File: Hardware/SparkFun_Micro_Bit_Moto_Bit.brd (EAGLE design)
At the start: 58.4 x 76.2 mm, 104 parts, among them J1 POWER_JACKPTH_LOCK, J2 CORTEX_DEBUGPTH, U1 CY8C4245LQI-483, U2 TPS62172, U3 micro:bit, U4 DRV8835

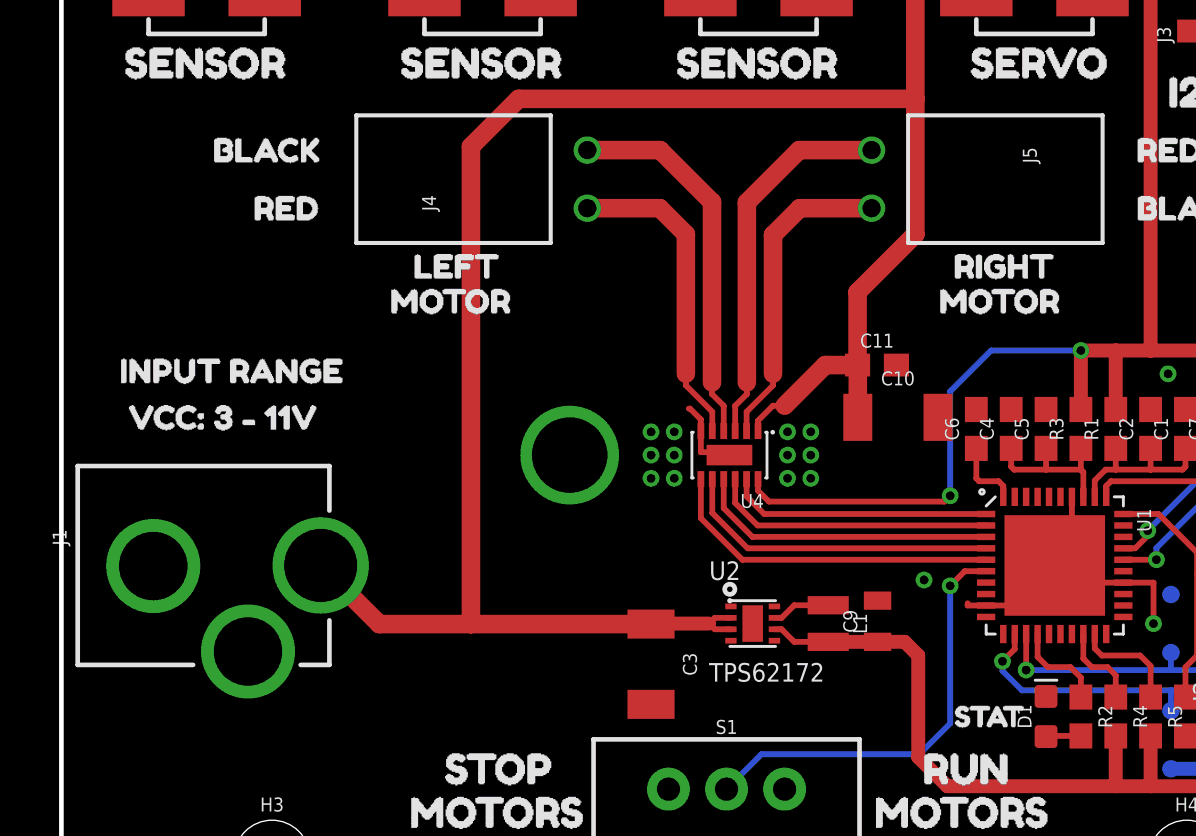
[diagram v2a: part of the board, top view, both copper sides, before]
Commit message: v20 update
Updated LED to current footprint and moved barrel connector in to reduce overhanging parts
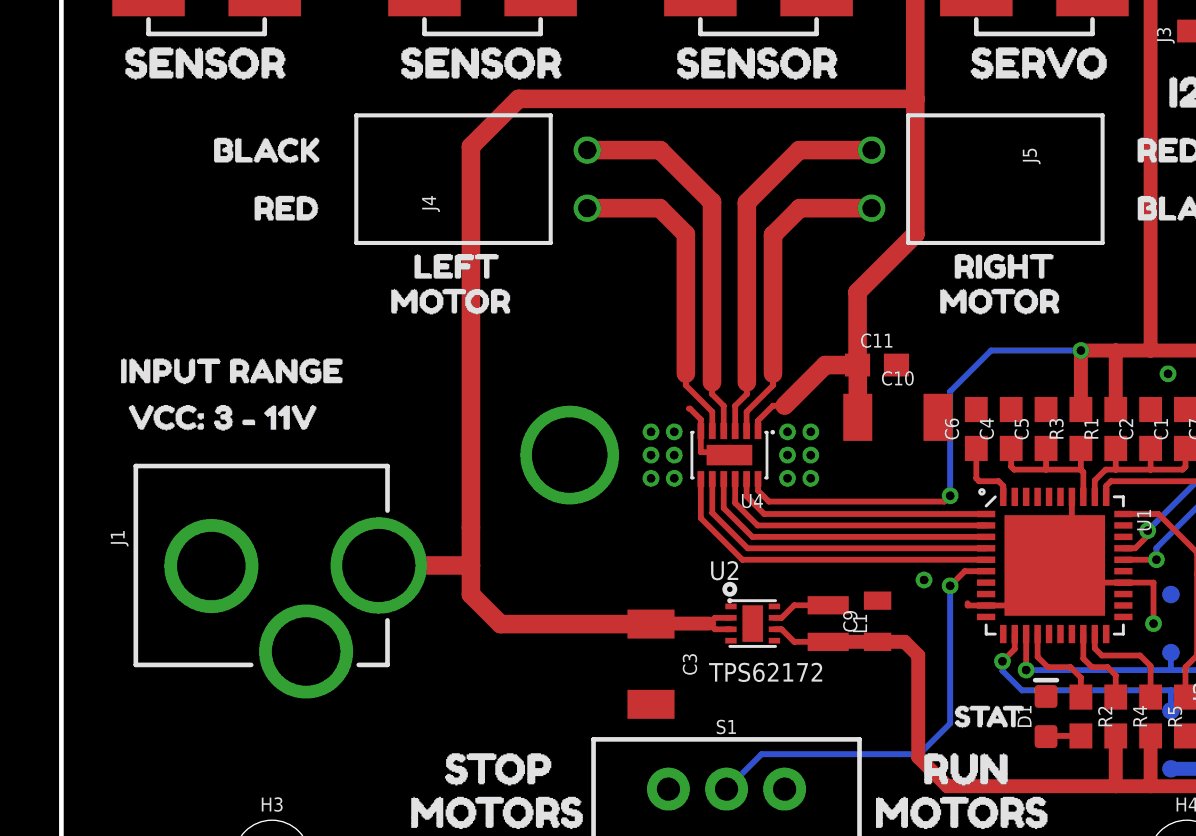
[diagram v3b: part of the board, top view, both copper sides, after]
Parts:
- moved J1 2.54 mm to (0.00, 18.7)
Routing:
- net VCC: track 95.9 -> 91.6 mm
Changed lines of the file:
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@@
 <layer number="38" name="bTest" color="7" fill="1" visible="no" active="yes"/>
 <layer number="39" name="tKeepout" color="4" fill="11" visible="yes" active="yes"/>
-<layer number="40" name="bKeepout" color="1" fill="11" visible="no" active="yes"/>
+<layer number="40" name="bKeepout" color="1" fill="11" visible="yes" active="yes"/>
 <layer number="41" name="tRestrict" color="4" fill="10" visible="no" active="yes"/>
 <layer number="42" name="bRestrict" color="1" fill="10" visible="no" active="yes"/>
@@
 <attribute name="VALUE" x="30.72" y="25.273" size="0.6096" layer="27" font="vector" ratio="20" rot="R180" align="top-left"/>
 </element>
-<element name="J1" library="SparkFun-Connectors" package="POWER_JACK_PTH_LOCK" value="POWER_JACKPTH_LOCK" x="-2.54" y="18.669" smashed="yes" rot="R270">
-<attribute name="NAME" x="-0.381" y="20.2438" size="0.6096" layer="25" font="vector" ratio="20" rot="R270"/>
-<attribute name="PROD_ID" value="CONN-08197" x="-27.94" y="56.769" size="1.778" layer="27" font="vector" ratio="15" rot="R270" display="off"/>
-<attribute name="SF_ID" value="PRT-00119" x="-27.94" y="56.769" size="1.778" layer="27" font="vector" ratio="15" rot="R270" display="off"/>
-<attribute name="VALUE" x="-1.397" y="20.574" size="0.6096" layer="27" font="vector" ratio="20" rot="R270"/>
+<element name="J1" library="SparkFun-Connectors" package="POWER_JACK_PTH_LOCK" value="POWER_JACKPTH_LOCK" x="0" y="18.669" smashed="yes" rot="R270">
+<attribute name="NAME" x="2.159" y="20.2438" size="0.6096" layer="25" font="vector" ratio="20" rot="R270"/>
+<attribute name="PROD_ID" value="CONN-08197" x="-25.4" y="56.769" size="1.778" layer="27" font="vector" ratio="15" rot="R270" display="off"/>
+<attribute name="SF_ID" value="PRT-00119" x="-25.4" y="56.769" size="1.778" layer="27" font="vector" ratio="15" rot="R270" display="off"/>
+<attribute name="VALUE" x="1.143" y="20.574" size="0.6096" layer="27" font="vector" ratio="20" rot="R270"/>
 </element>
 <element name="U2" library="SparkFun-IC-Power" package="WSON-8-PAD" value="TPS62172" x="30.226" y="16.129" smashed="yes" rot="R270">
@@
 <wire x1="37.338" y1="39.070753125" x2="19.990490625" y2="39.070753125" width="0.8128" layer="1"/>
 <wire x1="19.990490625" y1="39.070753125" x2="17.907" y2="36.9872625" width="0.8128" layer="1"/>
-<wire x1="17.907" y1="36.9872625" x2="17.907" y2="16.106" width="0.8128" layer="1"/>
+<wire x1="17.907" y1="36.9872625" x2="17.907" y2="20.32" width="0.8128" layer="1"/>
 <contactref element="J9" pad="4"/>
 <contactref element="C11" pad="1"/>
 <contactref element="U4" pad="1"/>
 <contactref element="C10" pad="1"/>
+<wire x1="25.781" y1="16.106" x2="19.2" y2="16.106" width="0.8128" layer="1"/>
+<wire x1="19.2" y1="16.106" x2="17.907" y2="17.399" width="0.8128" layer="1"/>
+<wire x1="17.907" y1="17.399" x2="17.907" y2="18.669" width="0.8128" layer="1"/>
 <wire x1="34.821" y1="27.432" x2="34.8116" y2="27.432" width="0.8128" layer="1"/>
 <wire x1="34.8116" y1="30.6206" x2="34.8116" y2="27.432" width="0.8128" layer="1"/>
@@
 <wire x1="37.338" y1="39.070753125" x2="37.338" y2="33.147" width="0.8128" layer="1"/>
 <wire x1="30.46" y1="25.002890625" x2="30.46" y2="24.545" width="0.254" layer="1"/>
-<wire x1="25.781" y1="16.106" x2="17.907" y2="16.106" width="0.8128" layer="1"/>
-<wire x1="11.3378" y1="18.669" x2="13.9008" y2="16.106" width="0.8128" layer="1"/>
-<wire x1="13.9008" y1="16.106" x2="17.907" y2="16.106" width="0.8128" layer="1"/>
 <wire x1="37.338" y1="33.147" x2="34.8116" y2="30.6206" width="0.8128" layer="1"/>
 <wire x1="40.005" y1="45.72" x2="45.085" y2="45.72" width="0.254" layer="1"/>
+<wire x1="13.8778" y1="18.669" x2="17.907" y2="18.669" width="0.8128" layer="1"/>
+<wire x1="17.907" y1="18.669" x2="17.907" y2="20.32" width="0.8128" layer="1"/>
 </signal>
 <signal name="U2.5">

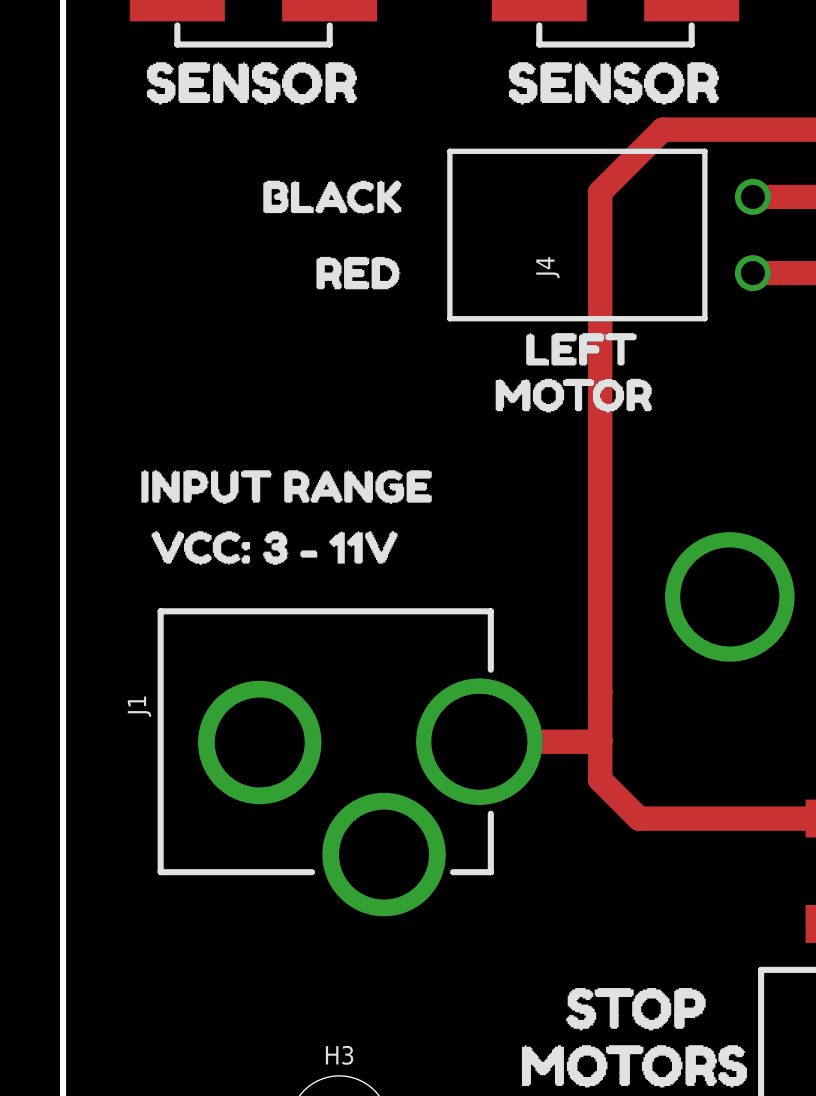
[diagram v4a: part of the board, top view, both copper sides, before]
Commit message: Update SparkFun_Micro_Bit_Moto_Bit.brd
Moved barrel jack in a little bit more for panelization.
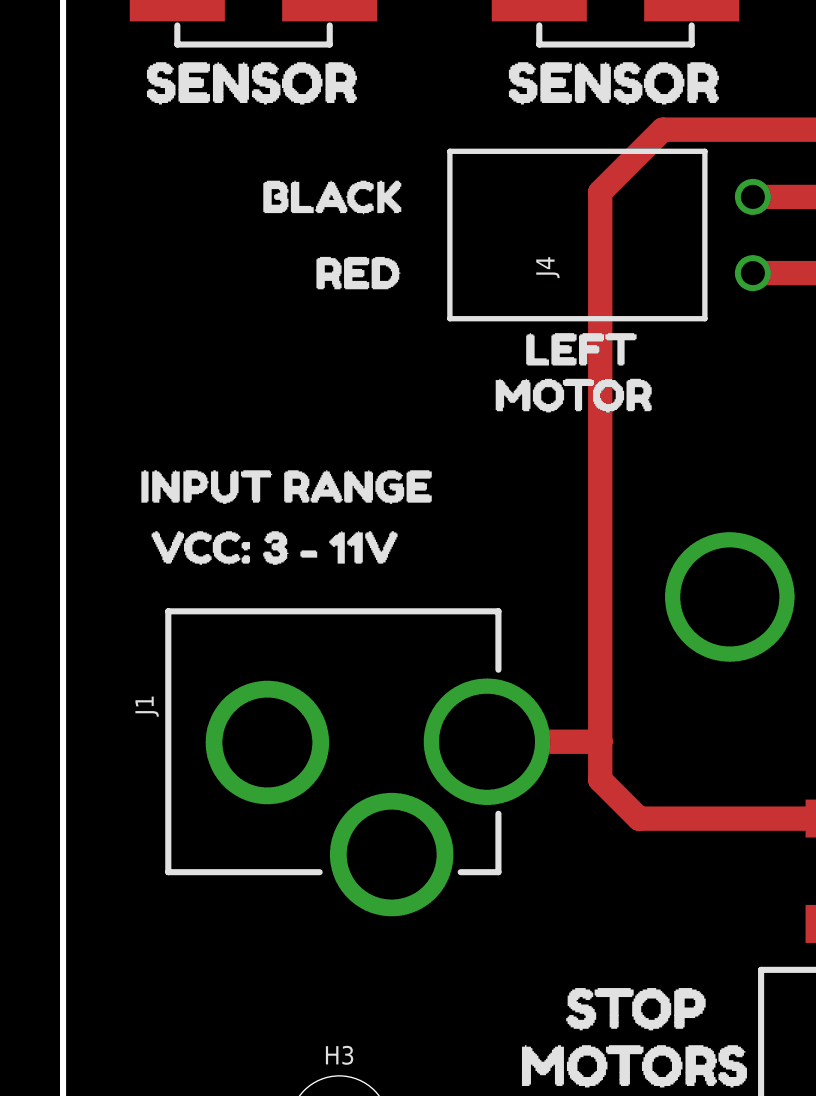
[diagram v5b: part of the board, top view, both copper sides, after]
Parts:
- moved J1 0.25 mm to (0.25, 18.7)
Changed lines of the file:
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@@
 <attribute name="VALUE" x="30.72" y="25.273" size="0.6096" layer="27" font="vector" ratio="20" rot="R180" align="top-left"/>
 </element>
-<element name="J1" library="SparkFun-Connectors" package="POWER_JACK_PTH_LOCK" value="POWER_JACKPTH_LOCK" x="0" y="18.669" smashed="yes" rot="R270">
-<attribute name="NAME" x="2.159" y="20.2438" size="0.6096" layer="25" font="vector" ratio="20" rot="R270"/>
-<attribute name="PROD_ID" value="CONN-08197" x="-25.4" y="56.769" size="1.778" layer="27" font="vector" ratio="15" rot="R270" display="off"/>
-<attribute name="SF_ID" value="PRT-00119" x="-25.4" y="56.769" size="1.778" layer="27" font="vector" ratio="15" rot="R270" display="off"/>
-<attribute name="VALUE" x="1.143" y="20.574" size="0.6096" layer="27" font="vector" ratio="20" rot="R270"/>
+<element name="J1" library="SparkFun-Connectors" package="POWER_JACK_PTH_LOCK" value="POWER_JACKPTH_LOCK" x="0.254" y="18.669" smashed="yes" rot="R270">
+<attribute name="NAME" x="2.413" y="20.2438" size="0.6096" layer="25" font="vector" ratio="20" rot="R270"/>
+<attribute name="PROD_ID" value="CONN-08197" x="-25.146" y="56.769" size="1.778" layer="27" font="vector" ratio="15" rot="R270" display="off"/>
+<attribute name="SF_ID" value="PRT-00119" x="-25.146" y="56.769" size="1.778" layer="27" font="vector" ratio="15" rot="R270" display="off"/>
+<attribute name="VALUE" x="1.397" y="20.574" size="0.6096" layer="27" font="vector" ratio="20" rot="R270"/>
 </element>
 <element name="U2" library="SparkFun-IC-Power" package="WSON-8-PAD" value="TPS62172" x="30.226" y="16.129" smashed="yes" rot="R270">
@@
 <wire x1="37.338" y1="39.070753125" x2="19.990490625" y2="39.070753125" width="0.8128" layer="1"/>
 <wire x1="19.990490625" y1="39.070753125" x2="17.907" y2="36.9872625" width="0.8128" layer="1"/>
-<wire x1="17.907" y1="36.9872625" x2="17.907" y2="20.32" width="0.8128" layer="1"/>
+<wire x1="17.907" y1="36.9872625" x2="17.907" y2="18.669" width="0.8128" layer="1"/>
 <contactref element="J9" pad="4"/>
 <contactref element="C11" pad="1"/>
@@
 <wire x1="37.338" y1="33.147" x2="34.8116" y2="30.6206" width="0.8128" layer="1"/>
 <wire x1="40.005" y1="45.72" x2="45.085" y2="45.72" width="0.254" layer="1"/>
-<wire x1="13.8778" y1="18.669" x2="17.907" y2="18.669" width="0.8128" layer="1"/>
-<wire x1="17.907" y1="18.669" x2="17.907" y2="20.32" width="0.8128" layer="1"/>
+<wire x1="14.1318" y1="18.669" x2="17.907" y2="18.669" width="0.8128" layer="1"/>
 </signal>
 <signal name="U2.5">

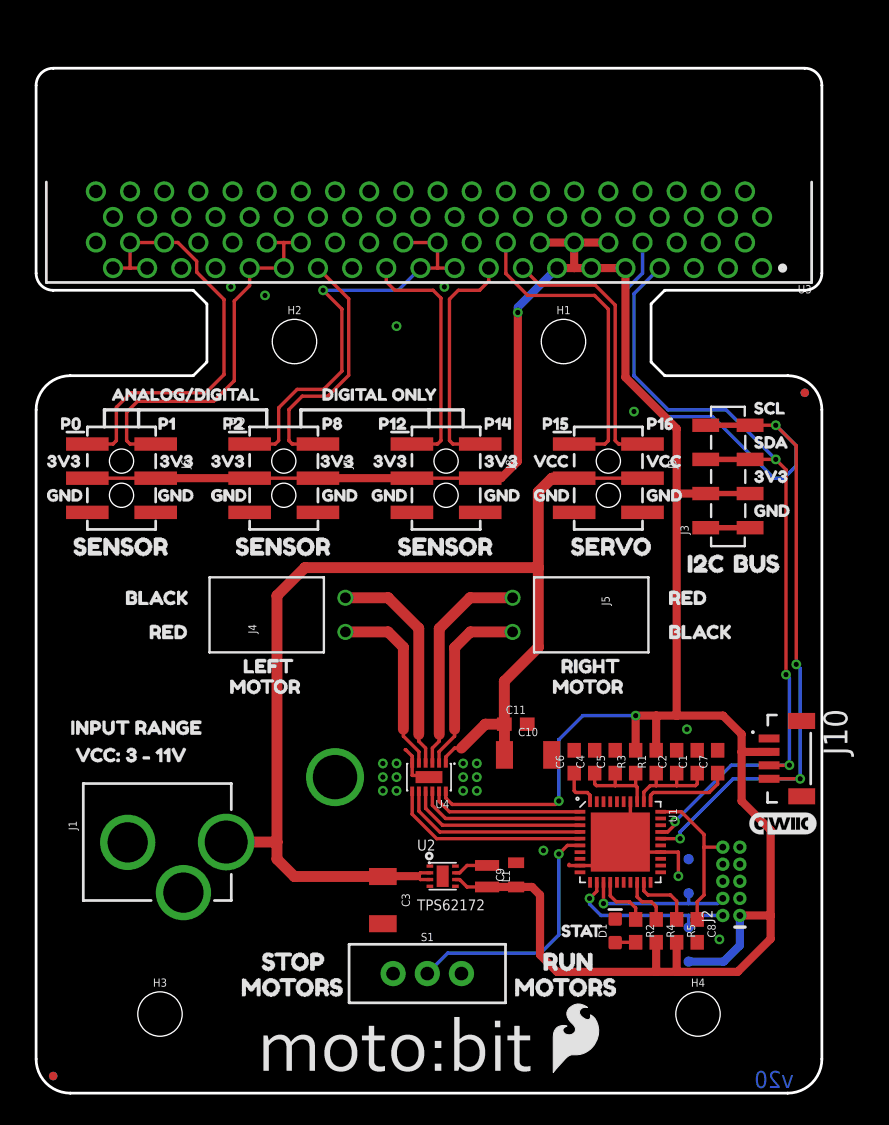
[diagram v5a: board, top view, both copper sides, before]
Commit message: v20_cont
Added micro:bit SMD footprint and test points.
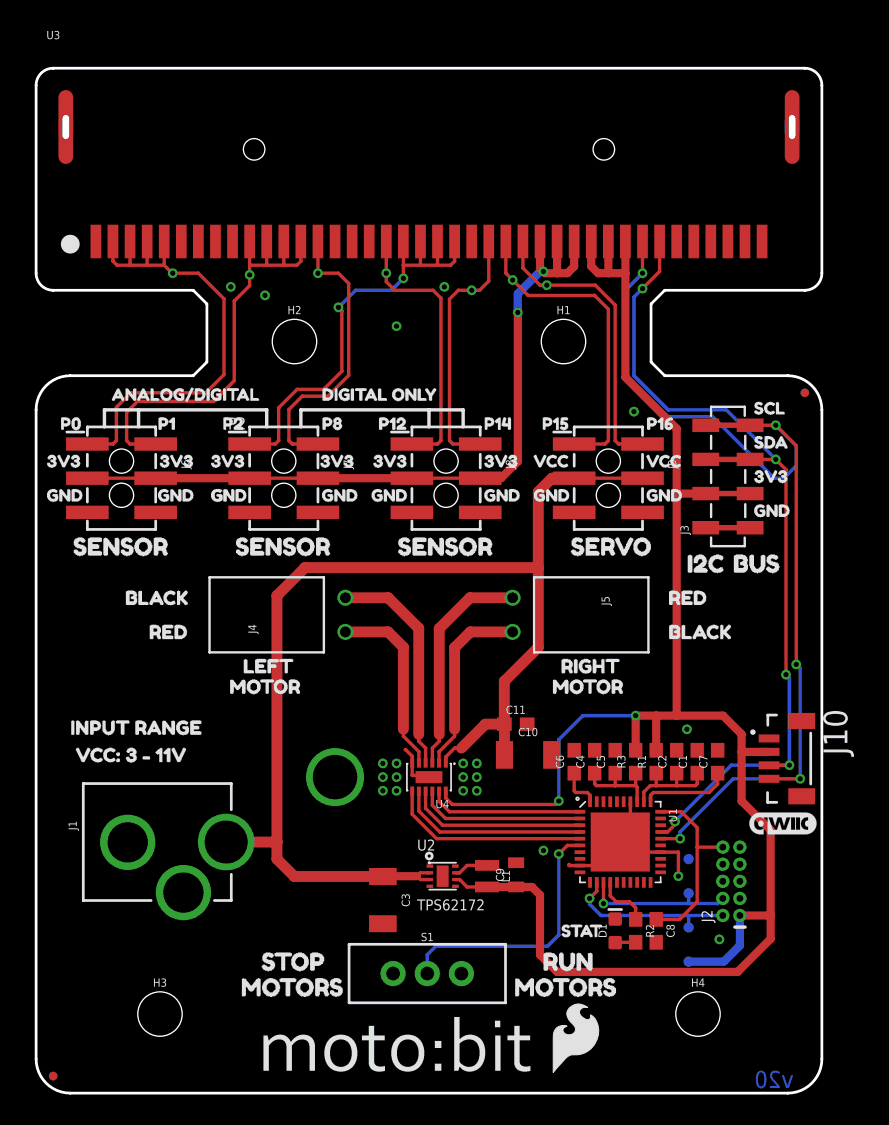
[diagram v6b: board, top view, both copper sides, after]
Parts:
- removed R4, R5: 4.7k, SparkFun-Resistors:0603
- added TP10, TP11, TP12, TP13, TP14, TP5, TP6, TP7, TP8, TP9: (no value), SparkFun-Connectors:TP_15TH
- J10: value (none) -> Qwiic
- J4, J5: device SparkFun-Connectors:1X02_RA_FEMALE -> SparkFun-Connectors:1X02_RA_PTH_FEMALE
- U3: device Micro_Bit_Parts:MICRO:BIT_RA_PTH -> SparkFun-Connectors:MICRO:BIT-RA_SMD
- moved C8 3.05 mm to (46.1, 12.1)
- moved TP1 2.54 mm to (48.5, 9.78)
- moved TP2 2.54 mm to (48.5, 17.4)
- moved TP3 2.54 mm to (48.5, 12.3)
- moved TP4 2.54 mm to (48.5, 14.9)
- moved U3 0.51 mm to (29.2, 69.5), turned to 0 degrees
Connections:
- removed net N$6: R4.1, U1.18
- removed net N$7: R5.1, U1.19
- net 3.3V: now also TP1.P$1, U3.P$27, U3.P$28, U3.P$29, U3.P$30, U3.P$31, U3.P$32; no longer R4.2, R5.2, TP3.P$1, U3.A10, U3.A11, U3.A12, U3.A13, U3.A14, U3.A9
- net ANALOG_0: now also TP5.P$1, U3.P$2, U3.P$3, U3.P$4, U3.P$5; no longer U3.A36, U3.A37, U3.A38, U3.A39
- net ANALOG_1: now also TP6.P$1, U3.P$10, U3.P$11, U3.P$12, U3.P$13; no longer U3.A28, U3.A29, U3.A30, U3.A31
- net ANALOG_2: now also TP8.P$1, U3.P$19, U3.P$20, U3.P$21, U3.P$22; no longer U3.A19, U3.A20, U3.A21, U3.A22
- net DIGITAL_12: now also TP9.P$1, U3.P$18; no longer U3.A23
- net DIGITAL_14: now also TP10.P$1, U3.P$24; no longer U3.A17
- net DIGITAL_8: now also TP7.P$1, U3.P$14; no longer U3.A27
- net GND: now also TP2.P$1, U3.P$35, U3.P$36, U3.P$37, U3.P$38, U3.P$39, U3.P$40; no longer TP4.P$1, U3.A1, U3.A2, U3.A3, U3.A4, U3.A5, U3.A6
- net P3.2: now also TP3.P$1; no longer TP1.P$1
- net P3.3: now also TP4.P$1; no longer TP2.P$1
- net SCL: now also TP13.P$1, U3.P$33; no longer U3.A8
- net SDA: now also TP14.P$1, U3.P$34; no longer U3.A7
- net SERVO_15: now also TP11.P$1, U3.P$25; no longer U3.A16
- net SERVO_16: now also TP12.P$1, U3.P$26; no longer U3.A15
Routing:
- net N$7: track 4.75 -> 0.00 mm
- net ANALOG_1: track 29.2 -> 33.2 mm
- net N$6: track 3.74 -> 0.00 mm
- net DIGITAL_8: track 19.0 -> 21.9 mm
- net ANALOG_0: track 33.0 -> 35.6 mm
- net !RESET: track 11.8 -> 14.2 mm
- net SERVO_16: track 20.2 -> 22.2 mm
- net DIGITAL_14: track 17.4 -> 19.3 mm
- net DIGITAL_12: track 18.4 -> 20.4 mm
- net SDA: track 60.3 -> 62.2 mm
- net 3.3V: track 192.3 -> 193.7 mm, vias 3 -> 4
- net U2.5: track 18.8 -> 19.6 mm
- net ANALOG_2: track 32.0 -> 32.8 mm
